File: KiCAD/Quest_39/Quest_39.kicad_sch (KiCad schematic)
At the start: 58 parts, among them J1 1x2 Scr. Term., J10 1x2 Scr. Term., J11 1x2 Scr. Term., J12 Conn_01x05_Male, J2 1x2 Scr. Term., J3 1x2 Scr. Term., J4 1x2 Scr. Term., J5 1x2 Scr. Term., J6 1x2 Scr. Term, J7 1x2 Scr. Term., J8 1x2 Scr. Term., J9 1x2 Scr. Term., U1 AZ1117-3.3, U2 17791063215, U3 STM32F103C8T6, Y1 16MHz

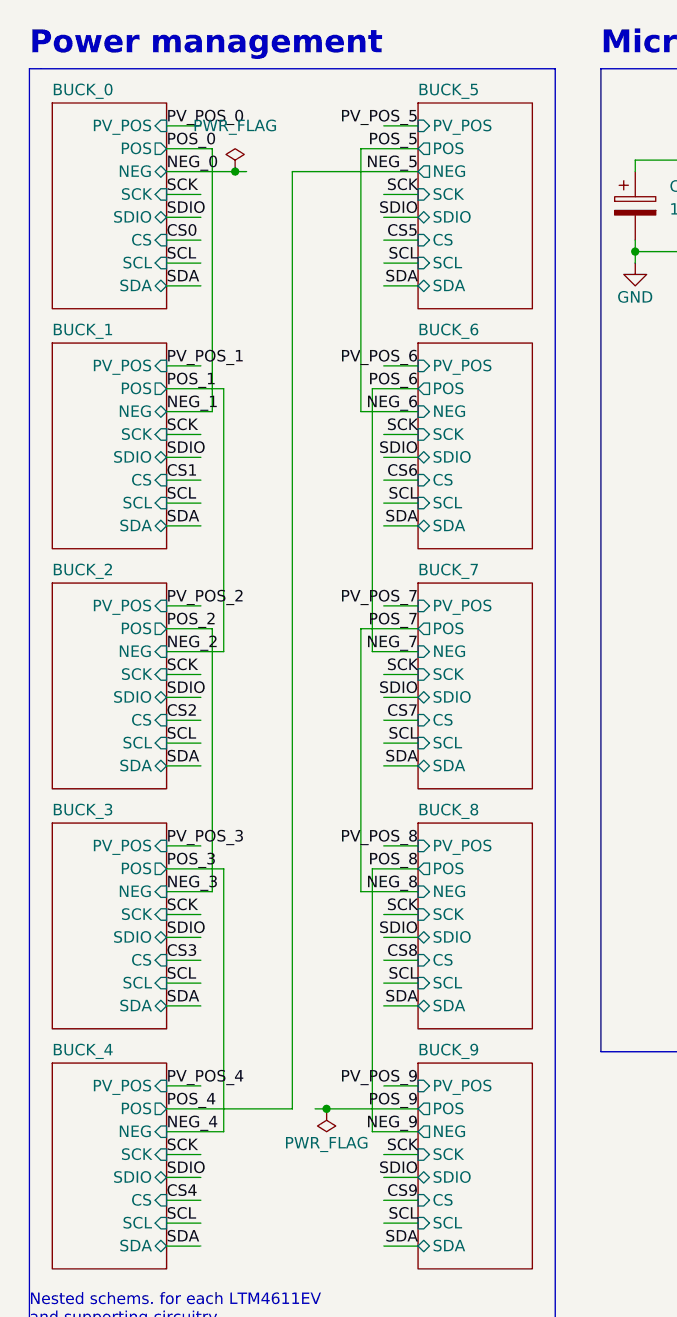
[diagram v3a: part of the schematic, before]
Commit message: Removed all ERC errors
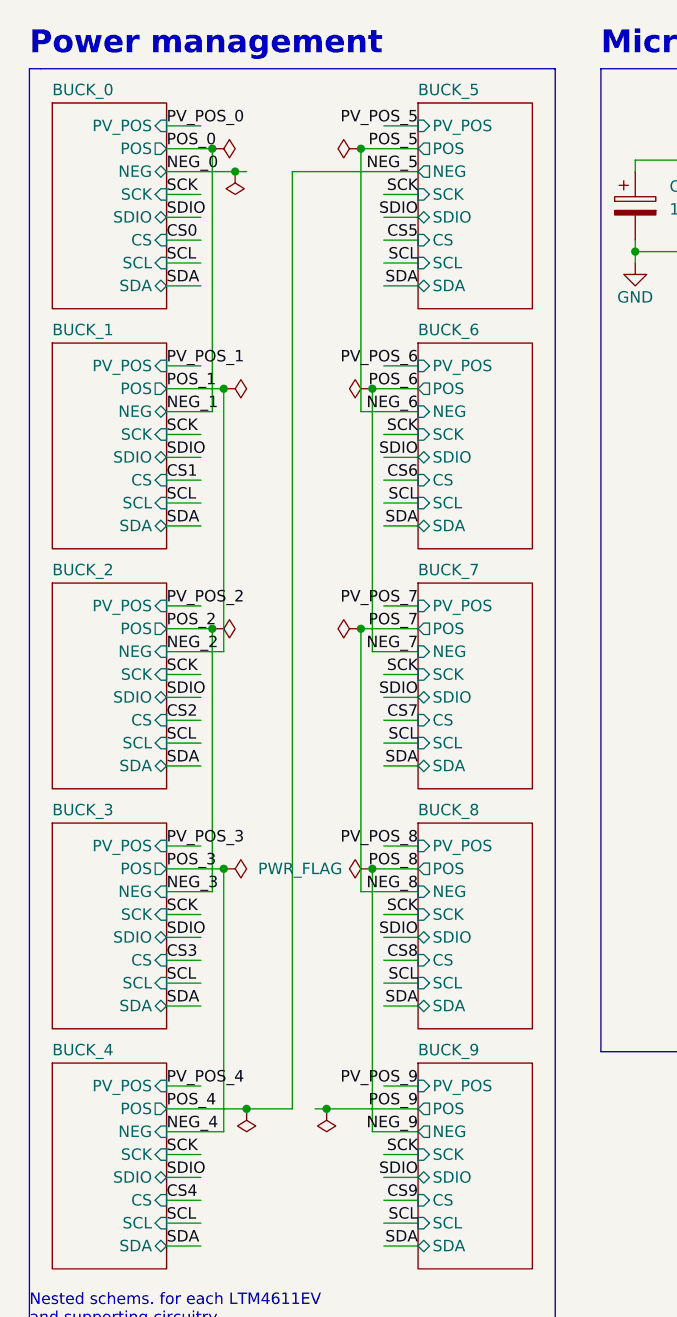
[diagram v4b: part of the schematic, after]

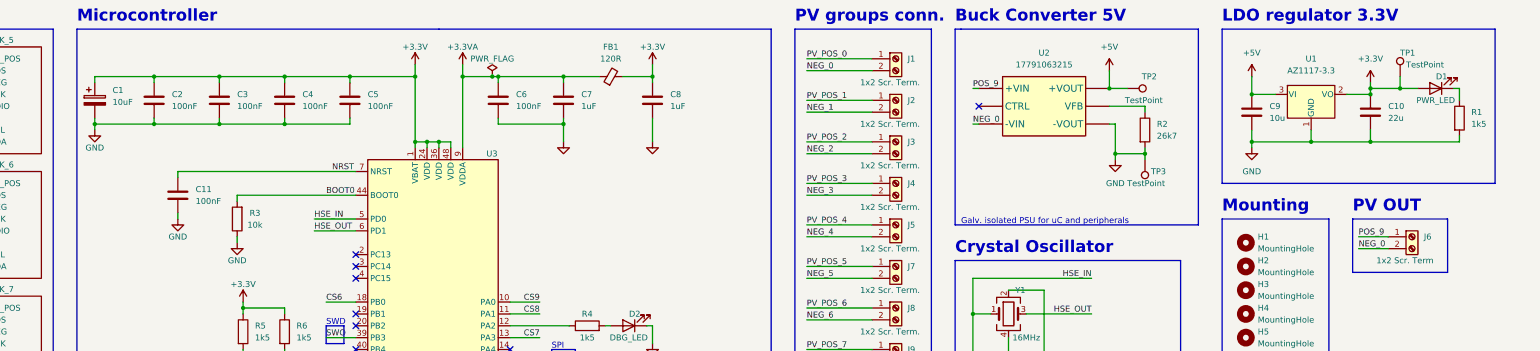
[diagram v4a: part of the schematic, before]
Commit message: Assigned all schem. symbols their footprints
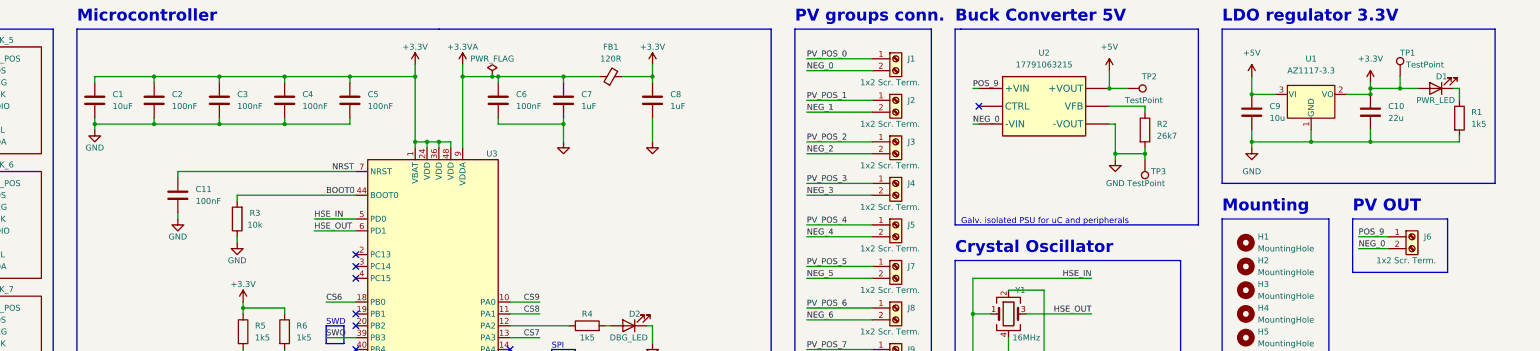
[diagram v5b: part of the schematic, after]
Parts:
- removed C1: 10uF, symbol Device:C_Polarized
- added C1: 10uF, Capacitor_SMD:C_0805_2012Metric, symbol Device:C
- C10, C11, C12, C13, C2, C3, C4, C5, C6, C7, C8, C9: footprint (none) -> Capacitor_SMD:C_0805_2012Metric
- D1, D2: footprint (none) -> LED_SMD:LED_1206_3216Metric
- FB1: footprint (none) -> Inductor_SMD:L_0805_2012Metric
- H1, H2, H3, H4, H5: footprint (none) -> MountingHole:MountingHole_3mm
- J1, J10, J11, J2, J3, J4, J5, J7, J8, J9: footprint (none) -> footprints:TB005-762-02BE
- J12: footprint (none) -> Connector_PinHeader_2.54mm:PinHeader_1x05_P2.54mm_Vertical
- J6: value 1x2 Scr. Term -> 1x2 Scr. Term.; footprint (none) -> footprints:TB005-762-02BE
- R1, R10, R11, R12, R13, R14, R15, R16, R2, R3, R4, R5, R6, R7, R8, R9: footprint (none) -> Resistor_SMD:R_1206_3216Metric
- TP1, TP2, TP3, TP4, TP5: footprint (none) -> TestPoint:TestPoint_Pad_D2.0mm
- U1: footprint (none) -> Package_TO_SOT_SMD:SOT-223-3_TabPin2
- U2: footprint (none) -> 17791063215:17791063215
- Y1: footprint (none) -> Crystal:Crystal_SMD_3225-4Pin_3.2x2.5mm
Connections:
- net +3.3V: now also C1.1
- net GND: now also C1.2

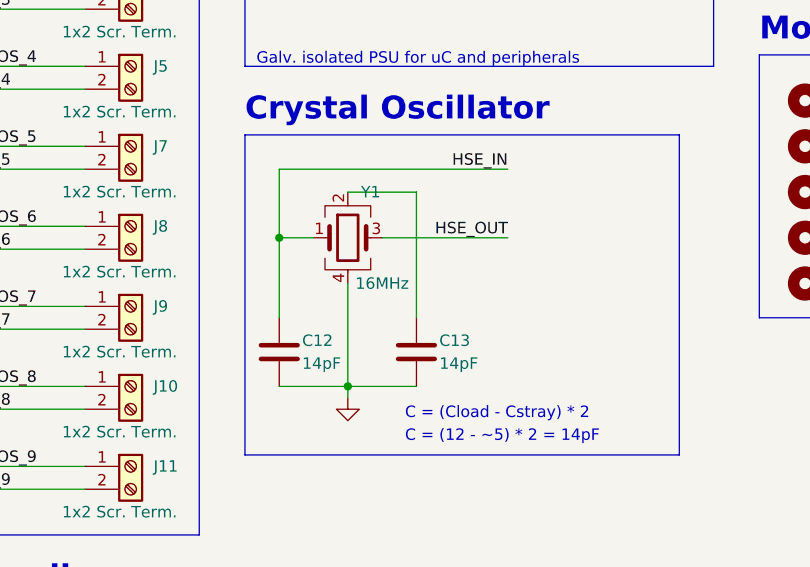
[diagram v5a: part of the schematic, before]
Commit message: Initial work on layout
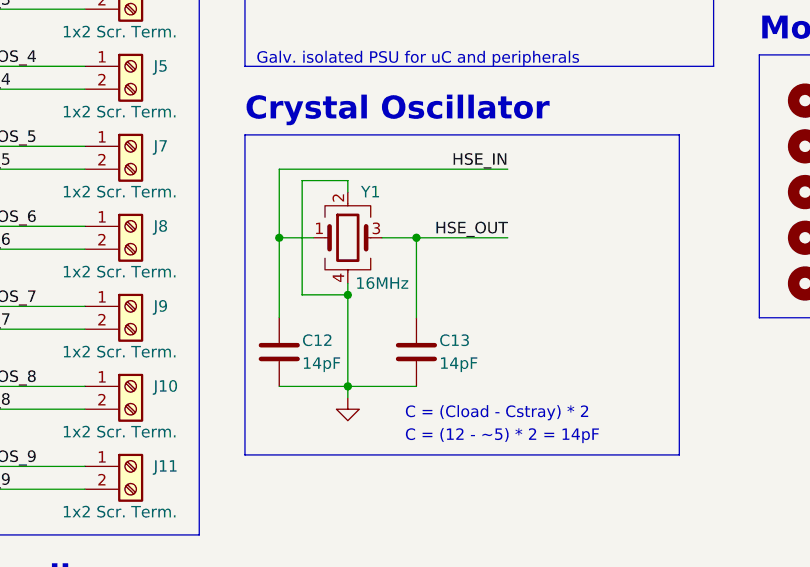
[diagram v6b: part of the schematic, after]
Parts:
- C1, C11, C12, C13, C2, C3, C4, C5, C6, C7, C8, C9: footprint Capacitor_SMD:C_0805_2012Metric -> Capacitor_SMD:C_0603_1608Metric
- FB1: footprint Inductor_SMD:L_0805_2012Metric -> Inductor_SMD:L_0603_1608Metric
- J1, J10, J11, J2, J3, J4, J5, J6, J7, J8, J9: footprint footprints:TB005-762-02BE -> TB005:TB005-762-02BE
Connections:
- net GND: now also Y1.2
- net HSE_OUT: now also C13.1
